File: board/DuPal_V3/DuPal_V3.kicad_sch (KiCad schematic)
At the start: 132 parts, among them J1 ZIF Socket, J2 Debug Header, J3 Extra, J4 Conn_01x21_Pin, J5 Conn_01x21_Pin, K1 G6K-2, Q1 2N3904, SW1 RESET, U1 Pico, U10 74HCT166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

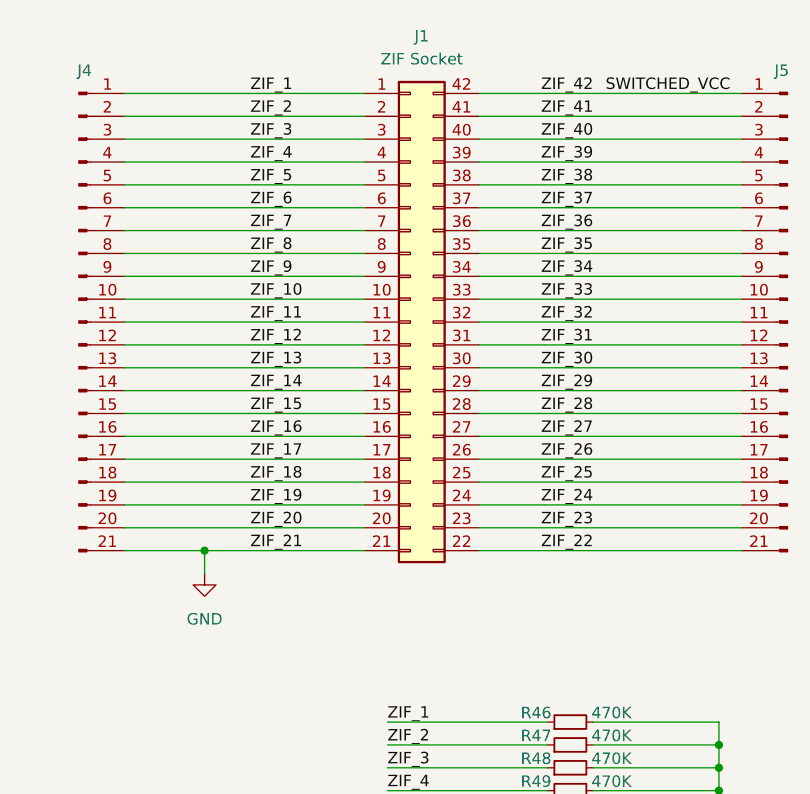
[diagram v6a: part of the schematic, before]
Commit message: Allow usage of a 48pin zif dip
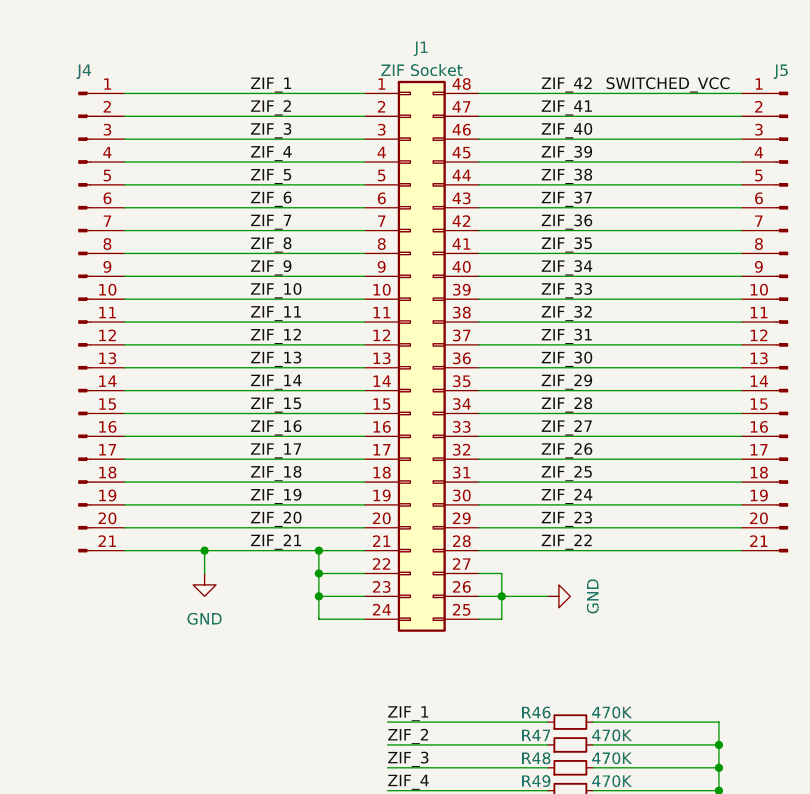
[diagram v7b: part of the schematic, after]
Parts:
- removed J1: ZIF Socket, Socket:DIP_Socket-42_W11.9_W12.7_W15.24_W17.78_W18.5_3M_242-1281-00-0602J, symbol Connector_Generic:Conn_02x21_Counter_Clockwise
- added J1: ZIF Socket, Custom_Sockets:DIP_Socket-48, symbol Connector_Generic:Conn_02x24_Counter_Clockwise
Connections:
- net GND: now also J1.21 (Pin_21), J1.22 (Pin_22), J1.23 (Pin_23), J1.24 (Pin_24), J1.25 (Pin_25), J1.26 (Pin_26), J1.27 (Pin_27)
- net SWITCHED_VCC: now also J1.48 (Pin_48)
- net ZIF_1: now also J1.1 (Pin_1)
- net ZIF_10: now also J1.10 (Pin_10)
- net ZIF_11: now also J1.11 (Pin_11)
- net ZIF_12: now also J1.12 (Pin_12)
- net ZIF_13: now also J1.13 (Pin_13)
- net ZIF_14: now also J1.14 (Pin_14)
- net ZIF_15: now also J1.15 (Pin_15)
- net ZIF_16: now also J1.16 (Pin_16)
- net ZIF_17: now also J1.17 (Pin_17)
- net ZIF_18: now also J1.18 (Pin_18)
- net ZIF_19: now also J1.19 (Pin_19)
- net ZIF_2: now also J1.2 (Pin_2)
- net ZIF_20: now also J1.20 (Pin_20)
- net ZIF_22: now also J1.28 (Pin_28)
- net ZIF_23: now also J1.29 (Pin_29)
- net ZIF_24: now also J1.30 (Pin_30)
- net ZIF_25: now also J1.31 (Pin_31)
- net ZIF_26: now also J1.32 (Pin_32)
- net ZIF_27: now also J1.33 (Pin_33)
- net ZIF_28: now also J1.34 (Pin_34)
- net ZIF_29: now also J1.35 (Pin_35)
- net ZIF_3: now also J1.3 (Pin_3)
- net ZIF_30: now also J1.36 (Pin_36)
- net ZIF_31: now also J1.37 (Pin_37)
- net ZIF_32: now also J1.38 (Pin_38)
- net ZIF_33: now also J1.39 (Pin_39)
- net ZIF_34: now also J1.40 (Pin_40)
- net ZIF_35: now also J1.41 (Pin_41)
- net ZIF_36: now also J1.42 (Pin_42)
- net ZIF_37: now also J1.43 (Pin_43)
- net ZIF_38: now also J1.44 (Pin_44)
- net ZIF_39: now also J1.45 (Pin_45)
- net ZIF_4: now also J1.4 (Pin_4)
- net ZIF_40: now also J1.46 (Pin_46)
- net ZIF_41: now also J1.47 (Pin_47)
- net ZIF_5: now also J1.5 (Pin_5)
- net ZIF_6: now also J1.6 (Pin_6)
- net ZIF_7: now also J1.7 (Pin_7)
- net ZIF_8: now also J1.8 (Pin_8)
- net ZIF_9: now also J1.9 (Pin_9)
